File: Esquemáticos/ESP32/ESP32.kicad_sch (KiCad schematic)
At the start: 1 part

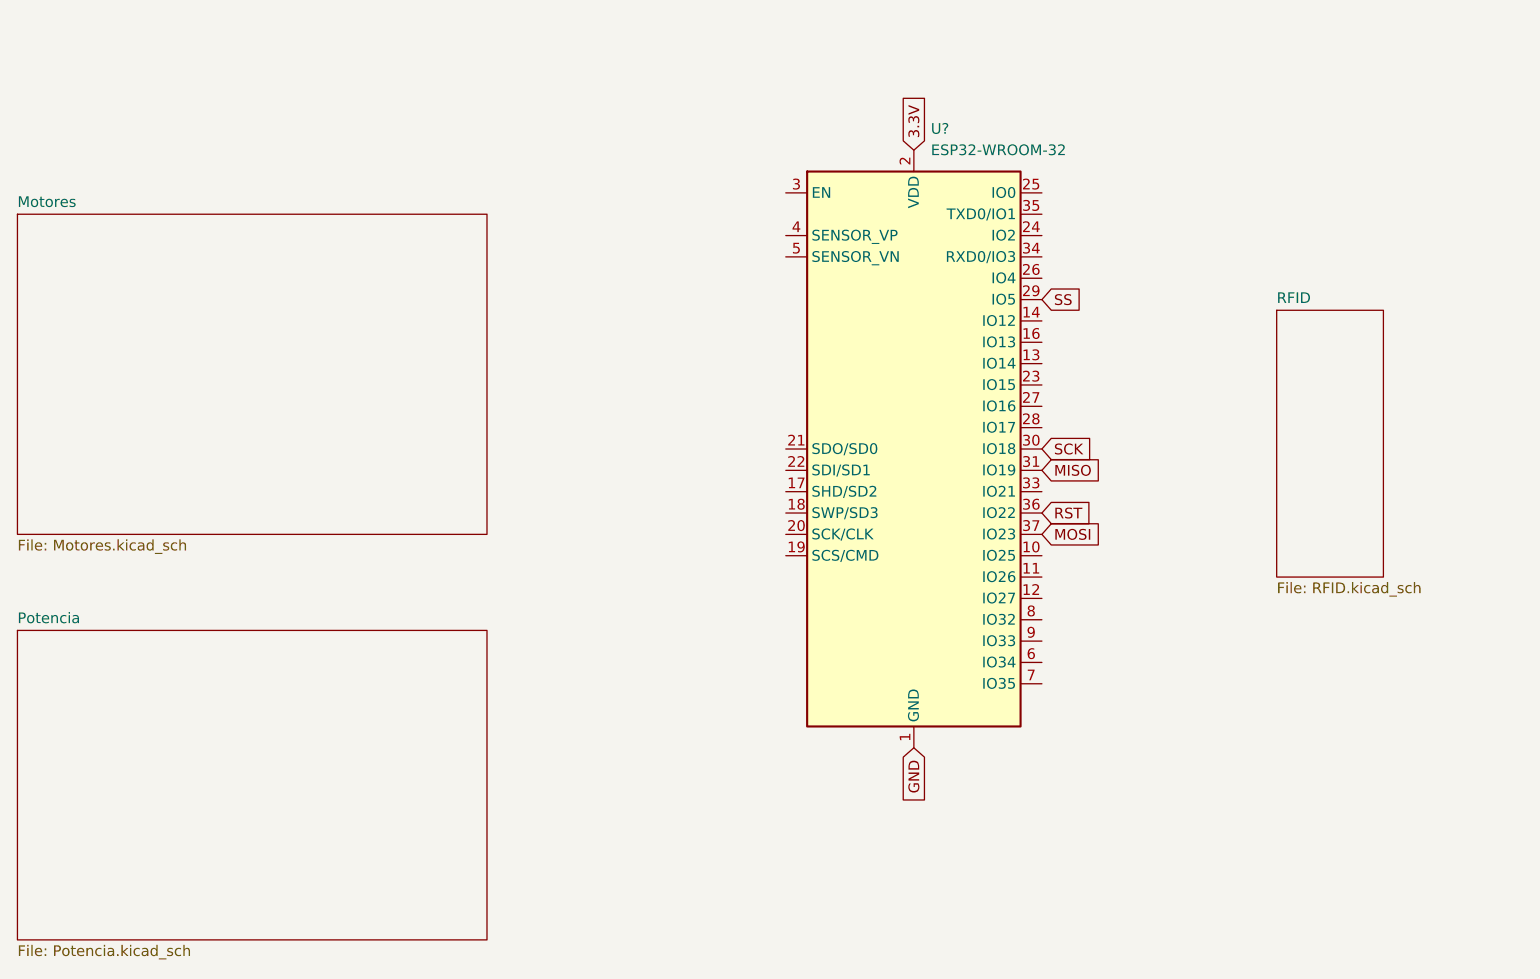
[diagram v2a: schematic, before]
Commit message: Añadido Modo Programación
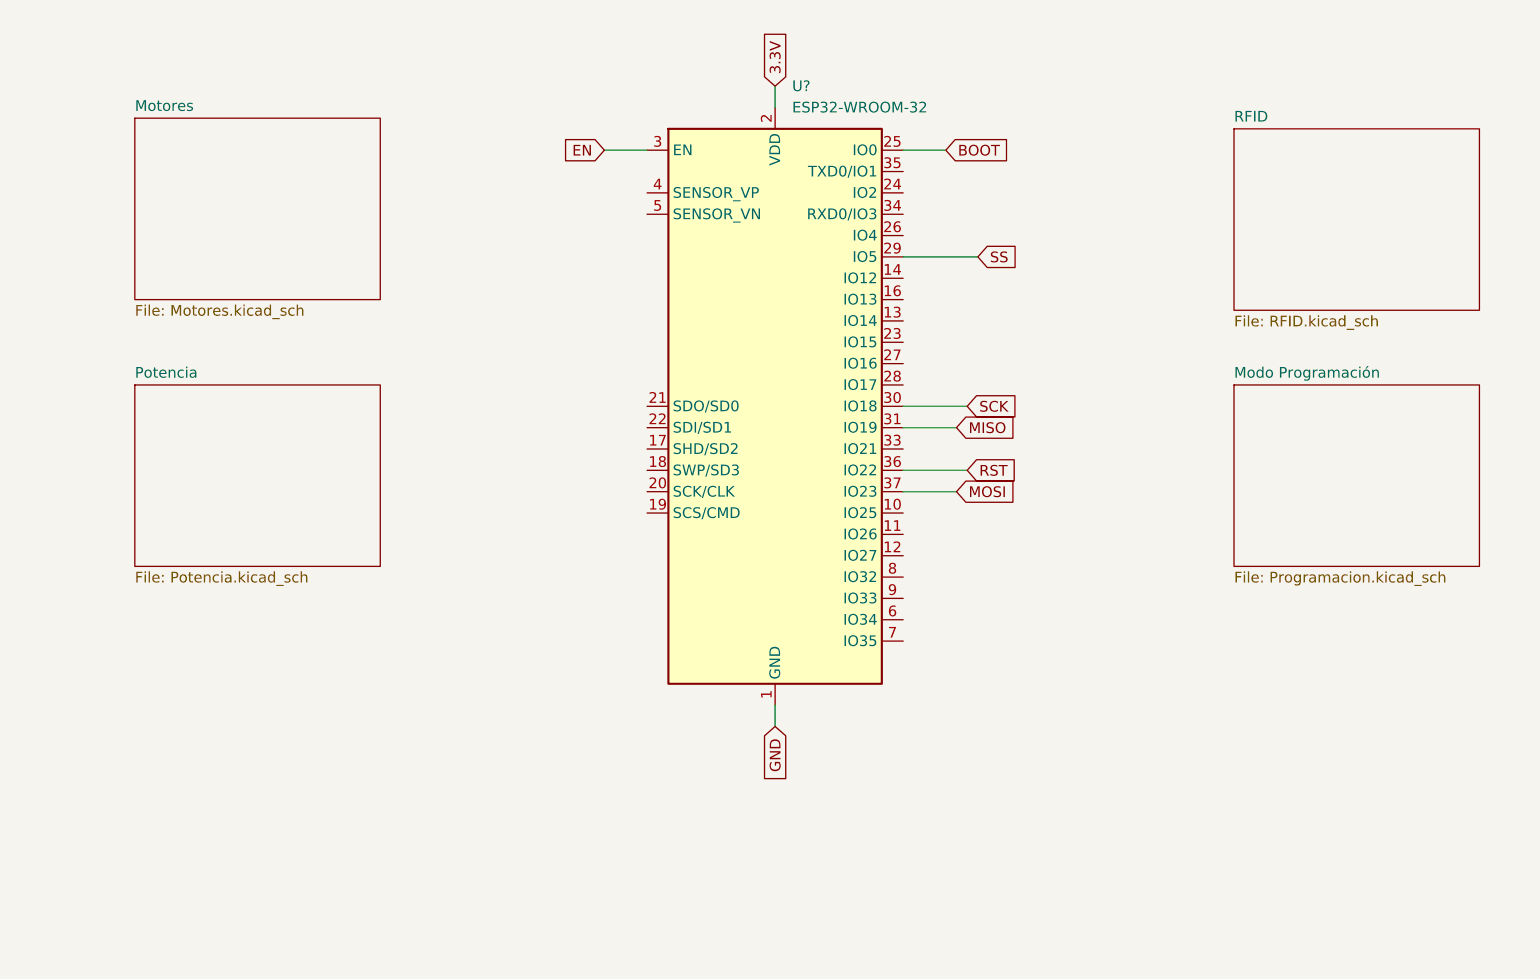
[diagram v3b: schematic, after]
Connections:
- net BOOT: now reaches U?.25 (IO0)
- net EN: now reaches U?.3 (EN)
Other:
- added sheet Modo Programación (Programacion.kicad_sch)
- moved on the sheet: U?

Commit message: Cambios hechos al esquemático, faltan detalles
Revisar el discord para dejar todo al día con el feedback de hoy
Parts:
- removed U?: ESP32-WROOM-32, RF_Module:ESP32-WROOM-32, symbol RF_Module:ESP32-WROOM-32
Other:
- sheet Modo Programación renamed Principal
- sheet Motores ports: added 12V, In1, In2, In3, In4; removed none
- sheet Potencia ports: added 12V, 3.3V, 5V; removed none
- sheet Principal ports: added 3.3V, BOOT, EN, MISO, MOSI, RST, SCK, SS; removed none
- sheet RFID ports: added 3.3V, MISO, MOSI, RST, SCK, SS; removed none
- note added: "Falta esto"
- note added: "esto que?xD"

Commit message: Actualizada la etapa de motores
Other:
- sheet Motores ports: added GNDL, In5, In6, In7, In8; removed none
- note added: "Revisar esto bien, porque no tiene sentido que el embebido con el lector de RFID esté en la misma PCB que el embebido para motores. Deberían ser 2 separadas. ¿Comunicación?"

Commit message: Intentando ponerle footprints a los motores
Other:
- note added: "Almacén"
- note added: "Interfaz"
- note added: "M1"
- note added: "M2"
- note added: "Motores"
- note added: "Módulo"
- note added: "O_O"
- note added: "Usuario"

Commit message: Arreglando los bugs xd
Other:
- note removed: "Almacén"
- note removed: "Interfaz"
- note removed: "M1"
- note removed: "M2"
- note removed: "Motores"
- note removed: "Módulo"
- note removed: "O_O"
- note removed: "Usuario"
